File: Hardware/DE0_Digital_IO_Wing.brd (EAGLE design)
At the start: 83.8 x 84.1 mm, 19 parts, among them J1 929975-01-20-RK, J2 929975-01-20-RK, J3 1-282834-0, J4 1-282834-0, J5 1-282834-0, J6 1-282834-0, U1 SN74LVC8T245PWR, U2 SN74LVC8T245PWR, U3 SN74LVC8T245PWR, U4 SN74LVC8T245PWR

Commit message: Working on layout.
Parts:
- added J7, J8: 1-282834-0, PP_Connectors:1-282834-0
- moved C3 181.7 mm to (85.6, 47.5)
- moved L3 164.6 mm to (90.7, 50.8)
- moved U3 164.4 mm to (85.6, 41.9)
- moved C1 152.1 mm to (85.6, 19.6)
- moved J5 145.3 mm to (100.8, 41.9), turned to 270 degrees
- moved C2 142.7 mm to (83.3, 5.59), turned to 270 degrees
- moved C4 133.6 mm to (55.1, 5.59), turned to 270 degrees
- moved L1 126.0 mm to (90.9, 22.9)
- moved L2 111.5 mm to (86.4, 1.02), turned to 270 degrees
- moved U4 110.7 mm to (49.5, 5.59), turned to 270 degrees
- moved L4 104.2 mm to (58.4, 1.52), turned to 270 degrees
- moved U2 100.0 mm to (77.5, 5.59), turned to 270 degrees
- moved U1 93.5 mm to (85.6, 14.0)
- moved J3 92.9 mm to (100.8, 14.0)
- moved J6 84.9 mm to (49.5, -8.89), turned to 180 degrees
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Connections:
- net GPIO0_D0: now also J7.P$8
- net GPIO0_D1: now also J7.P$7
- net GPIO0_D18: now also J8.P$6
- net GPIO0_D19: now also J8.P$5
- net GPIO0_D2: now also J7.P$9
- net GPIO0_D3: now also J7.P$10
- net GPIO0_D4: now also J8.P$1
- net GPIO0_D5: now also J8.P$2
- net GPIO0_D6: now also J8.P$4
- net GPIO0_D7: now also J8.P$3
- net GPIO1_D0: now also J7.P$1
- net GPIO1_D1: now also J7.P$2
- net GPIO1_D12: now also J8.P$8
- net GPIO1_D13: now also J8.P$7
- net GPIO1_D20: now also J8.P$9
- net GPIO1_D21: now also J8.P$10
- net GPIO1_D6: now also J7.P$3
- net GPIO1_D7: now also J7.P$4
- net GPIO1_D8: now also J7.P$6
- net GPIO1_D9: now also J7.P$5
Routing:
- net GPIO1_D24: track 0.00 -> 35.9 mm
- net GPIO1_D23: track 0.00 -> 34.4 mm
- net GPIO1_D26: track 0.00 -> 33.4 mm
- net GPIO1_D25: track 0.00 -> 31.9 mm
- net GPIO1_D28: track 0.00 -> 31.0 mm
- net GPIO1_D27: track 0.00 -> 29.4 mm
- net GPIO1_D30: track 0.00 -> 28.5 mm
- net GPIO1_D29: track 0.00 -> 27.0 mm
- net GPIO1_D31: track 0.00 -> 24.8 mm
- net AV: track 0.00 -> 22.7 mm
- net CV: track 0.00 -> 22.1 mm
- net BV: track 0.00 -> 20.9 mm
- net DV: track 0.00 -> 20.5 mm
- net C7: track 0.00 -> 16.0 mm
- net A7: track 0.00 -> 16.0 mm
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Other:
- board size 83.8 x 84.1 mm -> 105.9 x 84.1 mm

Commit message: REV0 preliminary complete.
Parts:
- moved FRAME 62.2 mm to (38.5, 14.7), turned to 90 degrees
- moved J7 47.0 mm to (44.5, 52.3)
- moved J8 38.0 mm to (71.4, 52.3)
- moved L1 18.4 mm to (107.2, 14.2), turned to 270 degrees
- moved C1 18.3 mm to (103.9, 19.6), turned to 270 degrees
- moved C2 15.2 mm to (77.2, 19.6)
- moved U2 15.2 mm to (71.4, 19.6)
- moved J4 15.0 mm to (71.4, 4.83)
- moved C4 14.9 mm to (50.0, 19.6)
- moved U4 14.9 mm to (44.5, 19.6)
- moved J6 14.6 mm to (44.5, 4.83)
- moved L2 14.5 mm to (80.3, 14.2)
- moved U1 13.9 mm to (98.3, 19.6), turned to 270 degrees
- moved L4 13.7 mm to (53.3, 14.2)
- moved U3 13.3 mm to (98.3, 38.1), turned to 90 degrees
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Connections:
- net 3.3V: no longer J1.29
- net 5.0V: no longer J2.11
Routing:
- net 3.3V: track 13.8 -> 323.2 mm
- net GPIO0_D8: track 0.00 -> 133.5 mm, vias 0 -> 1
- net GPIO0_D9: track 0.00 -> 121.1 mm, vias 0 -> 1
- net GPIO0_D14: track 0.00 -> 112.4 mm, vias 0 -> 1
- net GPIO0_D16: track 0.00 -> 110.7 mm, vias 0 -> 1
- net GPIO0_D15: track 0.00 -> 109.9 mm, vias 0 -> 1
- net GPIO0_D17: track 0.00 -> 106.9 mm, vias 0 -> 1
- net GPIO0_D20: track 0.00 -> 106.2 mm, vias 0 -> 1
- net GPIO0_D22: track 0.00 -> 106.0 mm, vias 0 -> 1
- net GPIO0_D23: track 0.00 -> 103.4 mm, vias 0 -> 1
- net GPIO0_D21: track 0.00 -> 103.1 mm, vias 0 -> 1
- net GPIO1_D21: track 0.00 -> 91.9 mm, vias 0 -> 1
- net GPIO0_D26: track 0.00 -> 89.2 mm, vias 0 -> 1
- net GPIO1_D20: track 0.00 -> 89.2 mm, vias 0 -> 1
- net GPIO0_D25: track 0.00 -> 88.7 mm, vias 0 -> 1
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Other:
- board size 105.9 x 84.1 mm -> 111.8 x 57.1 mm

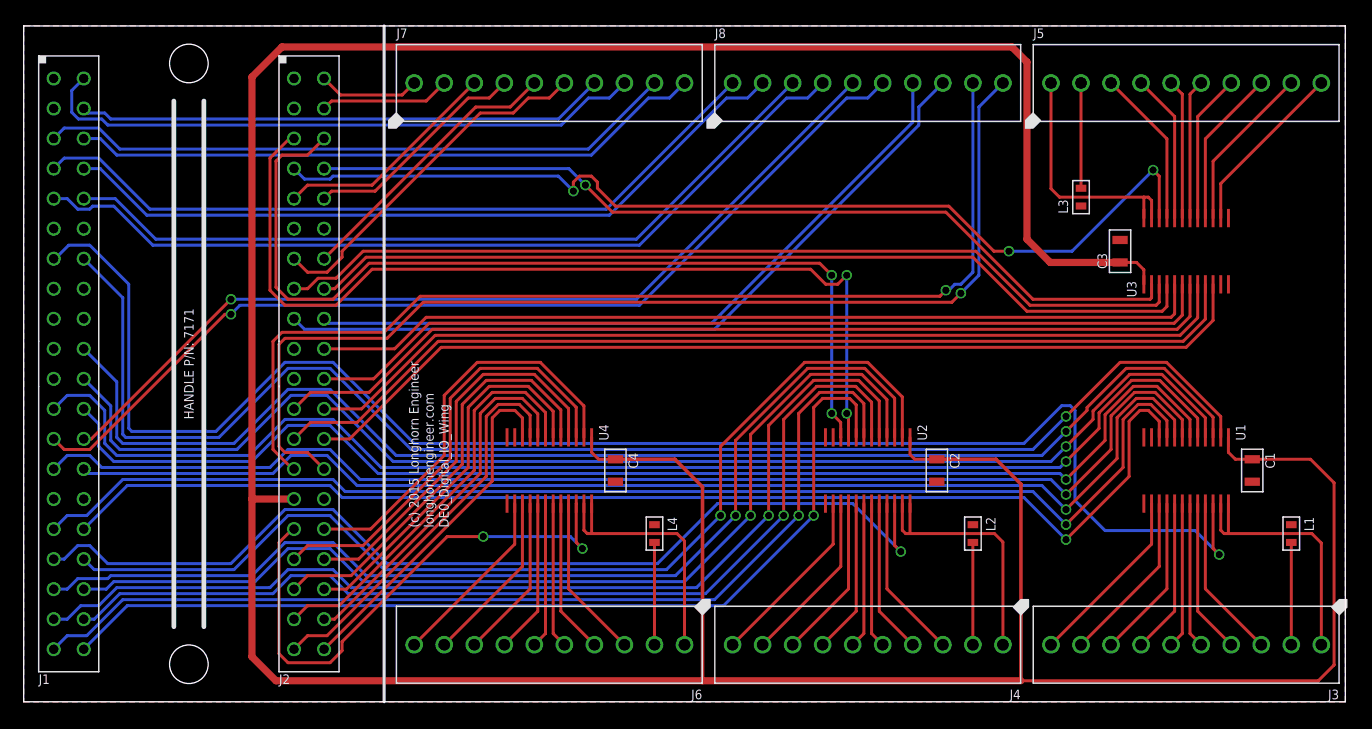
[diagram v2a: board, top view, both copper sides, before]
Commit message: Fixed some traces crossing gnd planes.
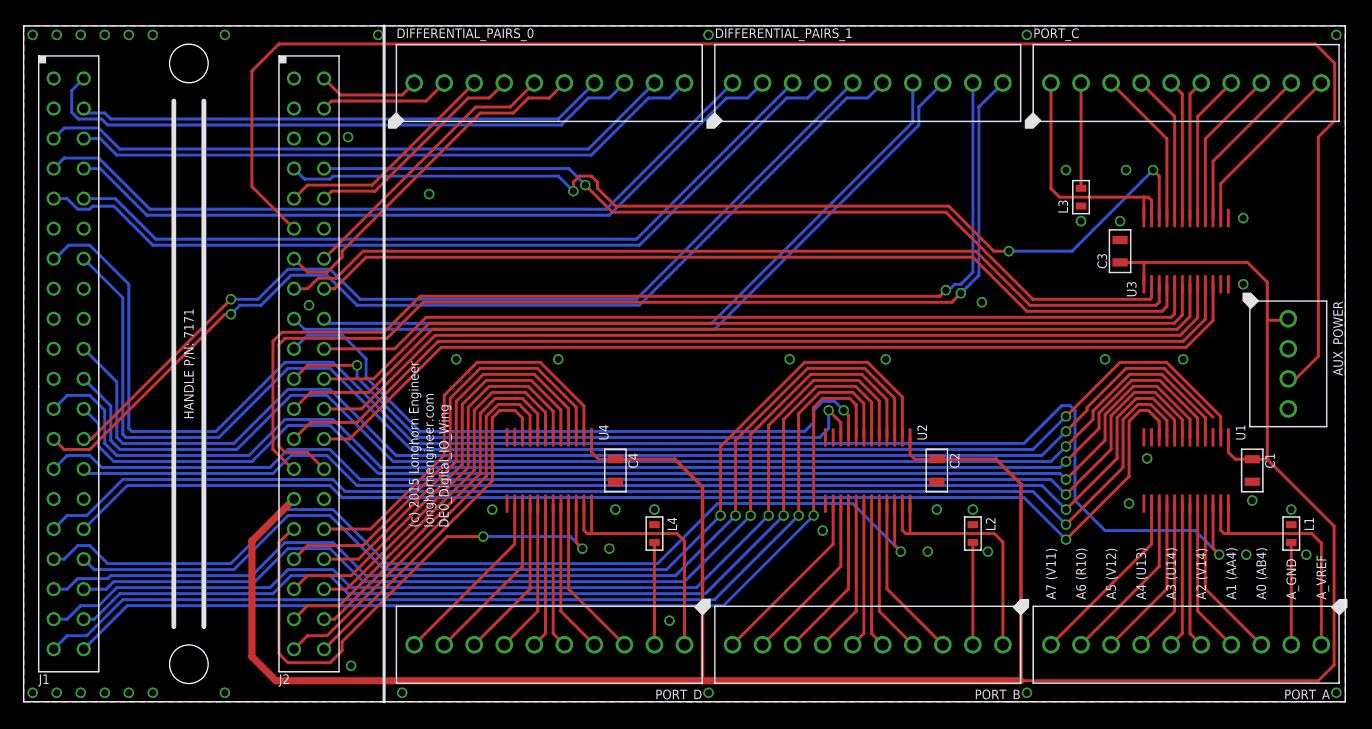
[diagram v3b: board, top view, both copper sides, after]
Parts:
- added AUX_POWER: 282834-4, PP_Connectors:282834-4
- renumbered J3 to PORT_A, J4 to PORT_B, J5 to PORT_C, J6 to PORT_D, J7 to DIFFERENTIAL_PAIRS_0, J8 to DIFFERENTIAL_PAIRS_1
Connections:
- net 3.3V: now also AUX_POWER.P$1
- net 5.0V: now also AUX_POWER.P$3, J2.11; no longer J1.11
- net DE0_GND: now also AUX_POWER.P$2, AUX_POWER.P$4
- net GPIO0_D14: no longer U1.P$3
- net GPIO1_CLKOUT0: now also U2.P$9
- net GPIO1_CLKOUT1: now also U2.P$10
- net GPIO1_D2: no longer U2.P$9
- net GPIO1_D3: no longer U2.P$10
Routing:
- net 5.0V: track 0.00 -> 136.7 mm
- net 3.3V: track 323.2 -> 220.8 mm
- net GPIO1_D2: track 79.1 -> 0.00 mm, vias 2 -> 0
- net GPIO1_D3: track 78.6 -> 0.00 mm, vias 2 -> 0
- net GPIO1_CLKOUT0: track 0.00 -> 55.7 mm, vias 0 -> 1
- net GPIO1_CLKOUT1: track 0.00 -> 53.4 mm, vias 0 -> 2
- net GPIO0_D18: track 83.6 -> 85.7 mm
- net GPIO0_D19: track 77.5 -> 79.6 mm
- net GPIO0_D14: track 112.4 -> 110.7 mm
